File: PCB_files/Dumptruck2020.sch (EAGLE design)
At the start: 16 parts, among them IC1 317EMP, Q1 N/A, Q2 N/A, Q3 N/A

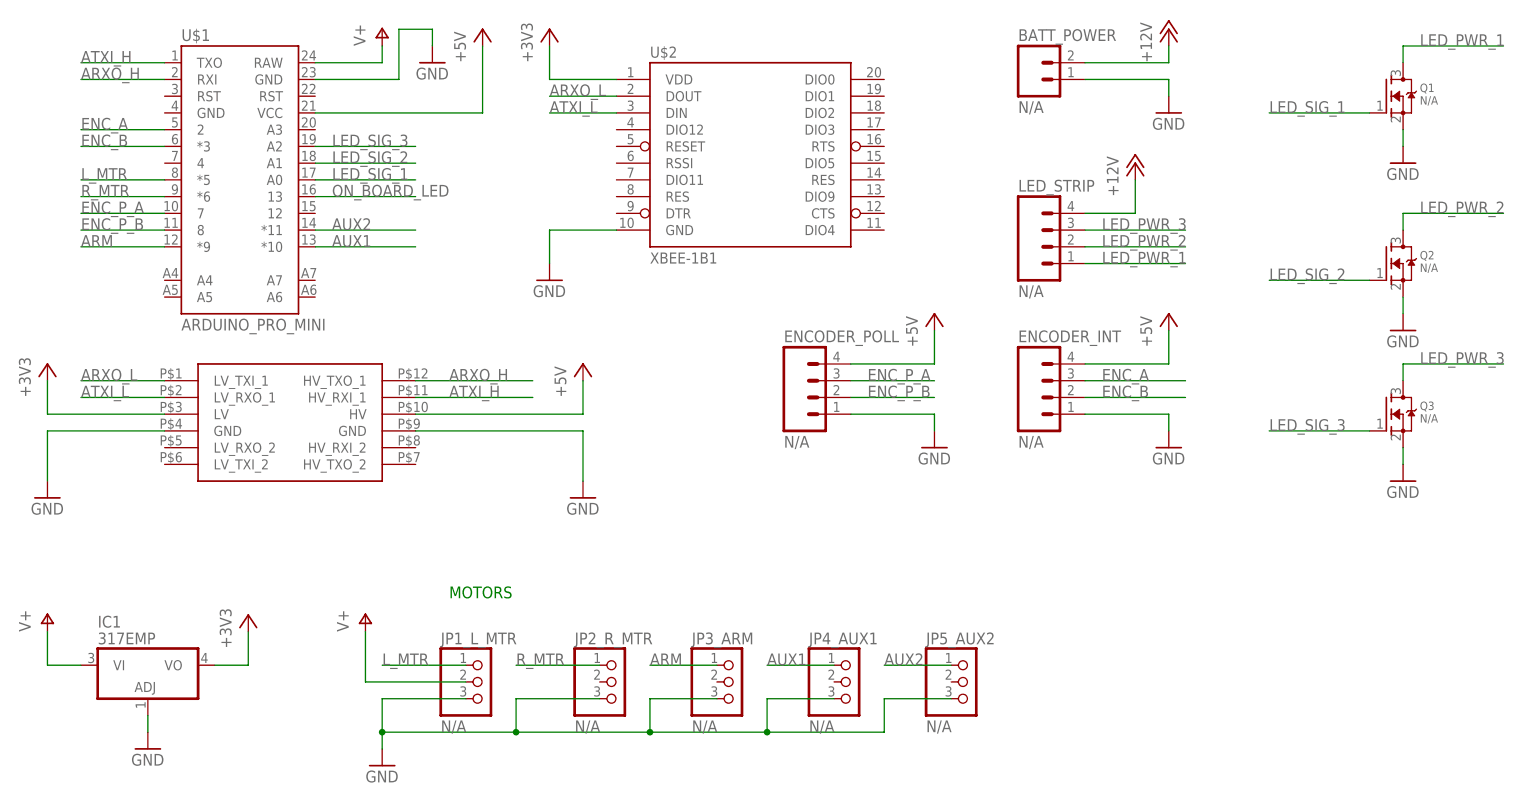
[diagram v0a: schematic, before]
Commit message: Adding 2020 New PCB Files
This commit adds the new 2020 Eagle files for the
"Controls" board. Features a new switch.
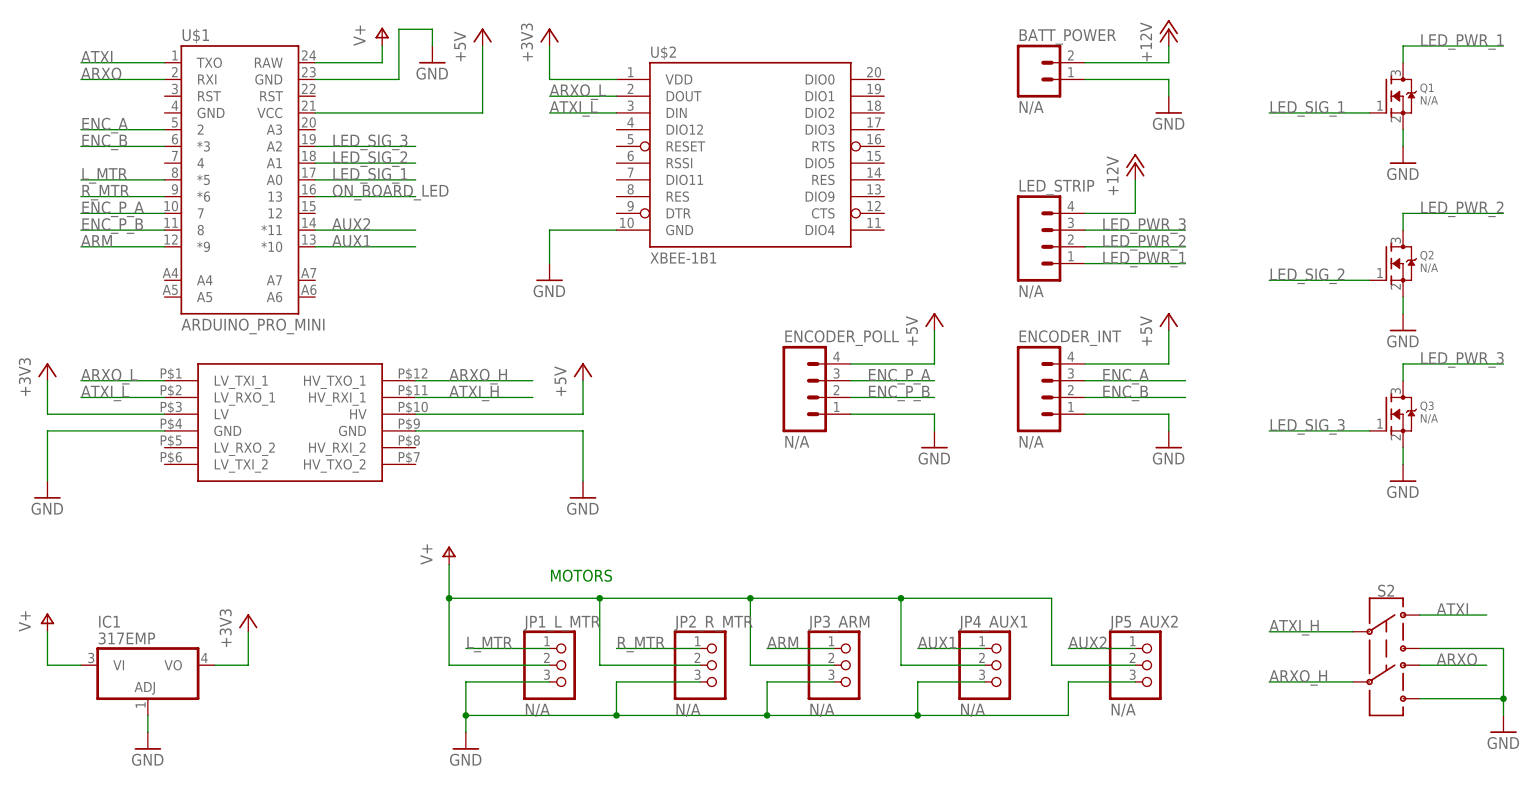
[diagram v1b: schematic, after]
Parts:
- added S2: (no value), SparkFun-Switches:SWITCH-DPDT-SMD-AYZ0202
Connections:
- new net ARXO: S2.4, U$1.RXI
- new net ATXI: S2.1, U$1.TXO
- net ARXO_H: now also S2.5; no longer U$1.RXI
- net ATXI_H: now also S2.2; no longer U$1.TXO
- net GND: now also S2.3, S2.6
- net V+: now also JP2_R_MTR.2, JP3_ARM.2, JP4_AUX1.2, JP5_AUX2.2
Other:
- moved on the sheet: JP1_L_MTR, JP2_R_MTR, JP3_ARM, JP4_AUX1, JP5_AUX2
